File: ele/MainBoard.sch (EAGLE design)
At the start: 129 parts, among them IC1 MCP23017SP, IC2 74HC595D, IC3 74HC595D, X1 POWER_IN, X10 M7, X2 POWER_OUT, X3 M2, X4 M4, X5 M6, X6 M8, X7 M1, X8 M3, X9 M5

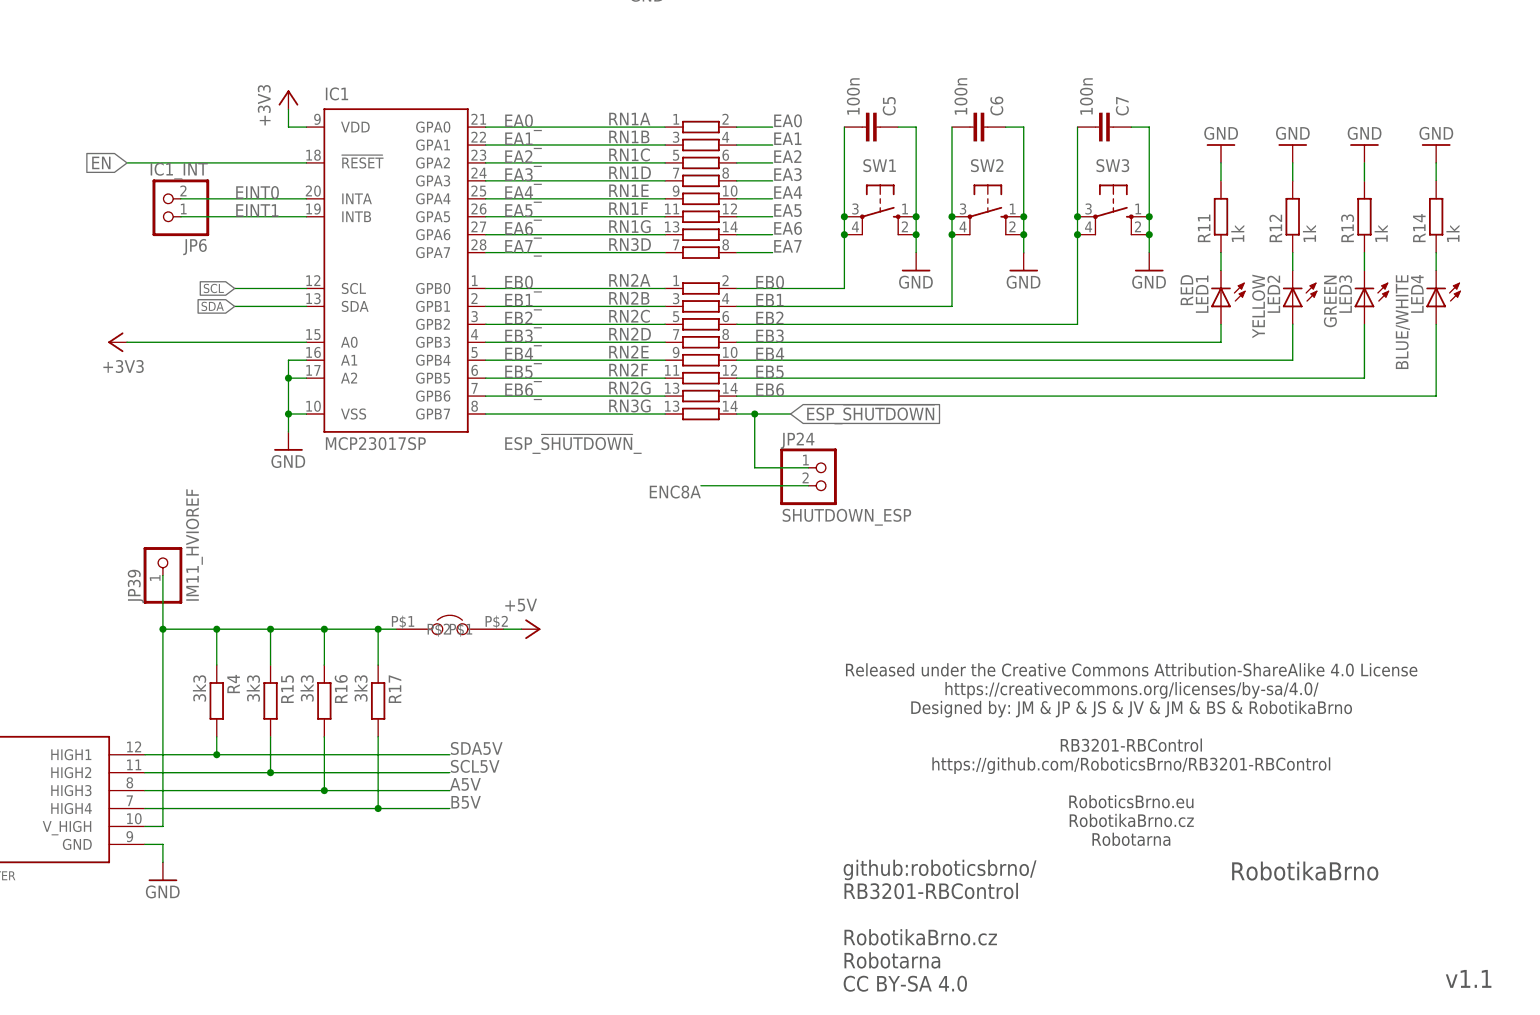
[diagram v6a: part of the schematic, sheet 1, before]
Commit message: ele: MainBoard - fix TO92 transistors pinout, change diodes package from SMD to TH, some signals routing improvements, fix some labels position, change version to 1.2
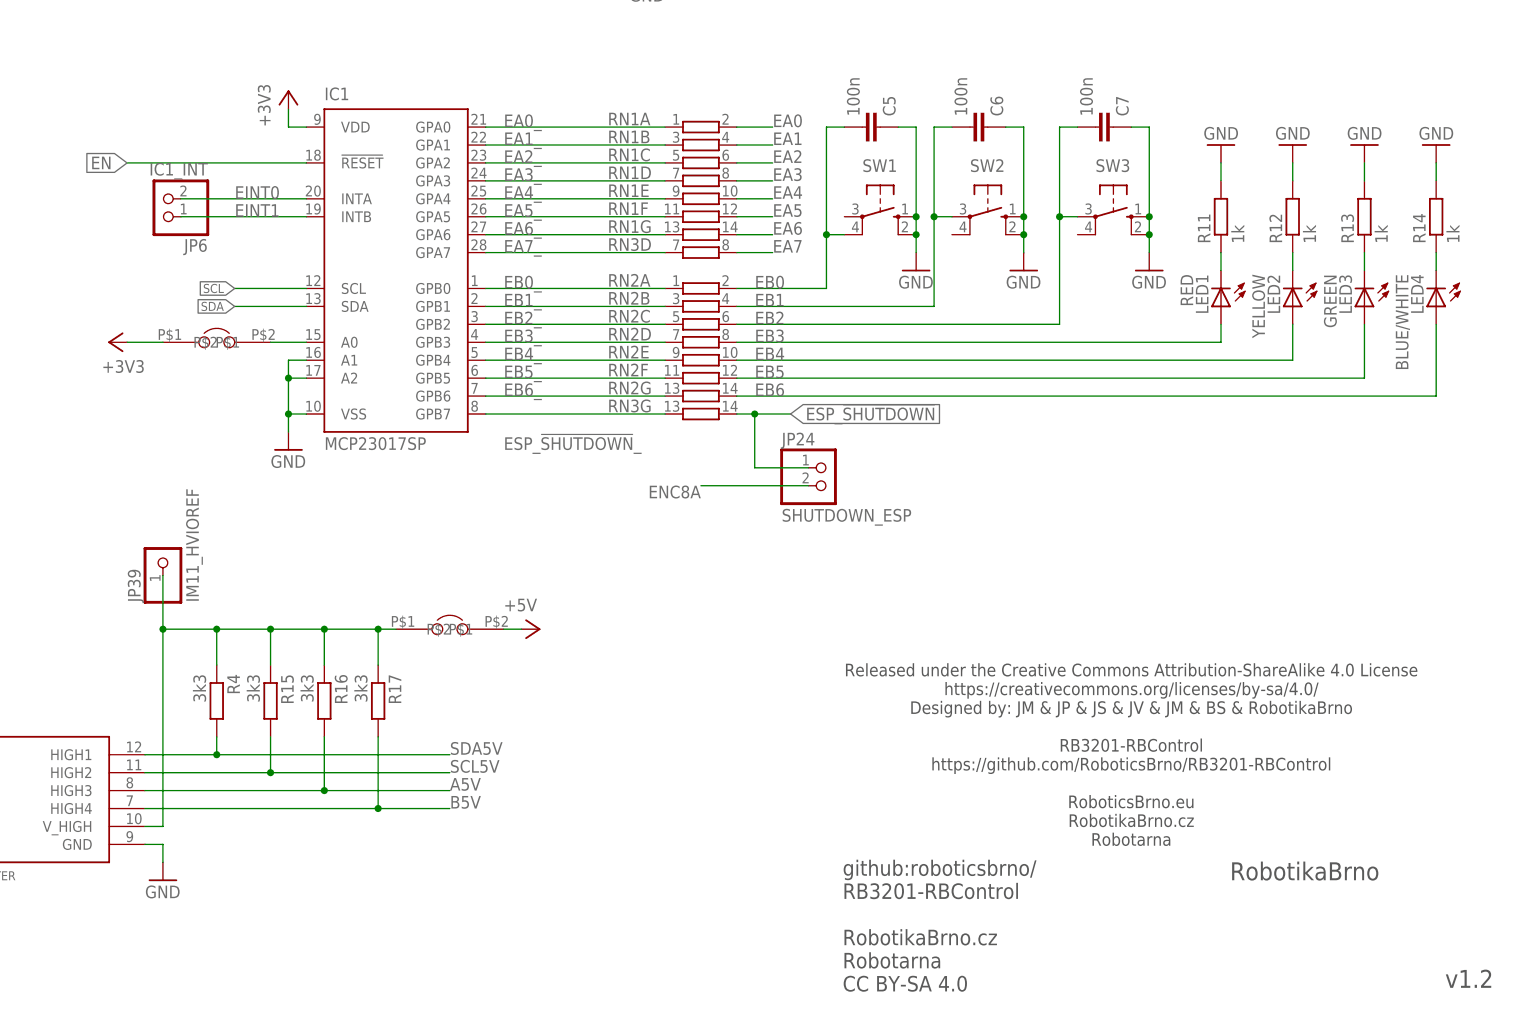
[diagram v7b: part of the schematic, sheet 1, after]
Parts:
- added U$1: SJ_NC, SolderJumperNormallyClosed:SJ_NC
- D1: device diode:DIODE-SOD123 -> diode:DIODE-D-2.5
- D2: device diode:DIODE-SOD123 -> diode:DIODE-D-7.5
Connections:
- new net EXP_A0: IC1.A0, U$1.P$2
- net +3V3: now also U$1.P$1; no longer IC1.A0
- net EB0: no longer SW1.P
- net EB1: no longer SW2.P1
- net EB2: no longer SW3.P1
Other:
- note added: "v1.2"

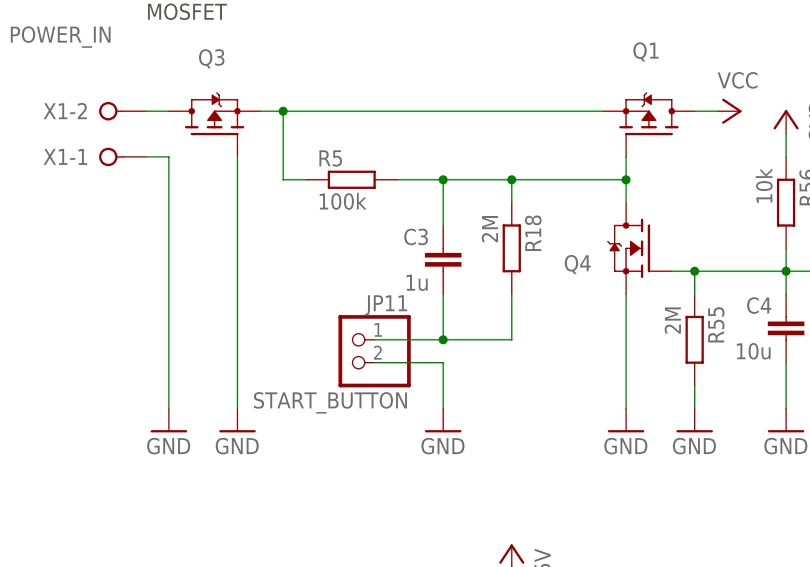
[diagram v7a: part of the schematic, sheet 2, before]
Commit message: ele: MainBoard - change value of C3 - from 1uF to 10uF
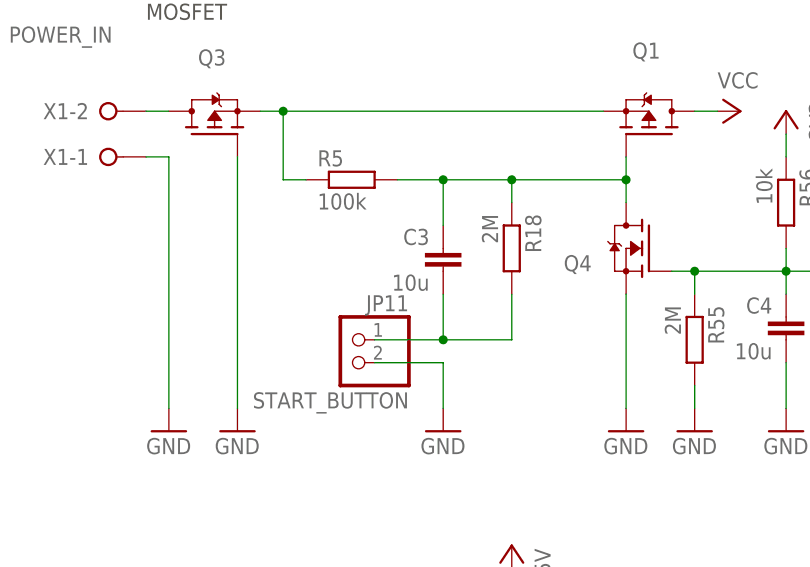
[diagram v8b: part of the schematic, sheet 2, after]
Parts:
- C3: value 1u -> 10u
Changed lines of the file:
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@@
 <grid distance="0.1" unitdist="inch" unit="inch" style="lines" multiple="1" display="no" altdistance="0.01" altunitdist="inch" altunit="inch"/>
 <layers>
-<layer number="1" name="Top" color="4" fill="1" visible="yes" active="no"/>
-<layer number="2" name="Route2" color="1" fill="3" visible="yes" active="no"/>
-<layer number="3" name="Route3" color="4" fill="3" visible="yes" active="no"/>
-<layer number="4" name="Route4" color="1" fill="4" visible="yes" active="no"/>
-<layer number="5" name="Route5" color="4" fill="4" visible="yes" active="no"/>
-<layer number="6" name="Route6" color="1" fill="8" visible="yes" active="no"/>
-<layer number="7" name="Route7" color="4" fill="8" visible="yes" active="no"/>
-<layer number="8" name="Route8" color="1" fill="2" visible="yes" active="no"/>
-<layer number="9" name="Route9" color="4" fill="2" visible="yes" active="no"/>
-<layer number="10" name="Route10" color="1" fill="7" visible="yes" active="no"/>
-<layer number="11" name="Route11" color="4" fill="7" visible="yes" active="no"/>
-<layer number="12" name="Route12" color="1" fill="5" visible="yes" active="no"/>
-<layer number="13" name="Route13" color="4" fill="5" visible="yes" active="no"/>
-<layer number="14" name="Route14" color="1" fill="6" visible="yes" active="no"/>
-<layer number="15" name="Route15" color="4" fill="6" visible="yes" active="no"/>
-<layer number="16" name="Bottom" color="1" fill="1" visible="yes" active="no"/>
-<layer number="17" name="Pads" color="2" fill="1" visible="yes" active="no"/>
-<layer number="18" name="Vias" color="2" fill="1" visible="yes" active="no"/>
-<layer number="19" name="Unrouted" color="6" fill="1" visible="yes" active="no"/>
-<layer number="20" name="Dimension" color="24" fill="1" visible="yes" active="no"/>
-<layer number="21" name="tPlace" color="7" fill="1" visible="yes" active="no"/>
-<layer number="22" name="bPlace" color="7" fill="1" visible="yes" active="no"/>
-<layer number="23" name="tOrigins" color="15" fill="1" visible="yes" active="no"/>
-<layer number="24" name="bOrigins" color="15" fill="1" visible="yes" active="no"/>
-<layer number="25" name="tNames" color="13" fill="1" visible="yes" active="no"/>
-<layer number="26" name="bNames" color="7" fill="1" visible="yes" active="no"/>
-<layer number="27" name="tValues" color="7" fill="1" visible="yes" active="no"/>
-<layer number="28" name="bValues" color="7" fill="1" visible="yes" active="no"/>
+<layer number="1" name="Top" color="4" fill="1" visible="no" active="no"/>
+<layer number="2" name="Route2" color="1" fill="3" visible="no" active="no"/>
+<layer number="3" name="Route3" color="4" fill="3" visible="no" active="no"/>
+<layer number="4" name="Route4" color="1" fill="4" visible="no" active="no"/>
+<layer number="5" name="Route5" color="4" fill="4" visible="no" active="no"/>
+<layer number="6" name="Route6" color="1" fill="8" visible="no" active="no"/>
+<layer number="7" name="Route7" color="4" fill="8" visible="no" active="no"/>
+<layer number="8" name="Route8" color="1" fill="2" visible="no" active="no"/>
+<layer number="9" name="Route9" color="4" fill="2" visible="no" active="no"/>
+<layer number="10" name="Route10" color="1" fill="7" visible="no" active="no"/>
+<layer number="11" name="Route11" color="4" fill="7" visible="no" active="no"/>
+<layer number="12" name="Route12" color="1" fill="5" visible="no" active="no"/>
+<layer number="13" name="Route13" color="4" fill="5" visible="no" active="no"/>
+<layer number="14" name="Route14" color="1" fill="6" visible="no" active="no"/>
+<layer number="15" name="Route15" color="4" fill="6" visible="no" active="no"/>
+<layer number="16" name="Bottom" color="1" fill="1" visible="no" active="no"/>
+<layer number="17" name="Pads" color="2" fill="1" visible="no" active="no"/>
+<layer number="18" name="Vias" color="2" fill="1" visible="no" active="no"/>
+<layer number="19" name="Unrouted" color="6" fill="1" visible="no" active="no"/>
+<layer number="20" name="Dimension" color="24" fill="1" visible="no" active="no"/>
+<layer number="21" name="tPlace" color="7" fill="1" visible="no" active="no"/>
+<layer number="22" name="bPlace" color="7" fill="1" visible="no" active="no"/>
+<layer number="23" name="tOrigins" color="15" fill="1" visible="no" active="no"/>
+<layer number="24" name="bOrigins" color="15" fill="1" visible="no" active="no"/>
+<layer number="25" name="tNames" color="13" fill="1" visible="no" active="no"/>
+<layer number="26" name="bNames" color="7" fill="1" visible="no" active="no"/>
+<layer number="27" name="tValues" color="7" fill="1" visible="no" active="no"/>
+<layer number="28" name="bValues" color="7" fill="1" visible="no" active="no"/>
 <layer number="29" name="tStop" color="7" fill="3" visible="no" active="no"/>
 <layer number="30" name="bStop" color="7" fill="6" visible="no" active="no"/>
@@
 <layer number="35" name="tGlue" color="7" fill="4" visible="no" active="no"/>
 <layer number="36" name="bGlue" color="7" fill="5" visible="no" active="no"/>
-<layer number="37" name="tTest" color="7" fill="1" visible="yes" active="no"/>
-<layer number="38" name="bTest" color="7" fill="1" visible="yes" active="no"/>
+<layer number="37" name="tTest" color="7" fill="1" visible="no" active="no"/>
+<layer number="38" name="bTest" color="7" fill="1" visible="no" active="no"/>
 <layer number="39" name="tKeepout" color="4" fill="11" visible="no" active="no"/>
 <layer number="40" name="bKeepout" color="1" fill="11" visible="no" active="no"/>
@@
 <layer number="44" name="Drills" color="7" fill="1" visible="no" active="no"/>
 <layer number="45" name="Holes" color="7" fill="1" visible="no" active="no"/>
-<layer number="46" name="Milling" color="3" fill="1" visible="yes" active="no"/>
-<layer number="47" name="Measures" color="7" fill="1" visible="yes" active="no"/>
-<layer number="48" name="Document" color="7" fill="1" visible="yes" active="no"/>
-<layer number="49" name="Reference" color="7" fill="1" visible="yes" active="no"/>
-<layer number="50" name="dxf" color="7" fill="1" visible="yes" active="no"/>
-<layer number="51" name="tDocu" color="7" fill="1" visible="yes" active="no"/>
-<layer number="52" name="bDocu" color="7" fill="1" visible="yes" active="no"/>
-<layer number="53" name="tGND_GNDA" color="7" fill="9" visible="yes" active="no"/>
-<layer number="54" name="bGND_GNDA" color="1" fill="9" visible="yes" active="no"/>
-<layer number="55" name="tPotisk" color="7" fill="1" visible="yes" active="no"/>
-<layer number="56" name="wert" color="7" fill="1" visible="yes" active="no"/>
-<layer number="57" name="tCAD" color="7" fill="1" visible="yes" active="no"/>
-<layer number="58" name="bNC" color="7" fill="1" visible="yes" active="no"/>
-<layer number="59" name="tCarbon" color="7" fill="1" visible="yes" active="no"/>
-<layer number="60" name="bCarbon" color="7" fill="1" visible="yes" active="no"/>
-<layer number="61" name="stand" color="7" fill="1" visible="yes" active="no"/>
+<layer number="46" name="Milling" color="3" fill="1" visible="no" active="no"/>
+<layer number="47" name="Measures" color="7" fill="1" visible="no" active="no"/>
+<layer number="48" name="Document" color="7" fill="1" visible="no" active="no"/>
+<layer number="49" name="Reference" color="7" fill="1" visible="no" active="no"/>
+<layer number="50" name="dxf" color="7" fill="1" visible="no" active="no"/>
+<layer number="51" name="tDocu" color="7" fill="1" visible="no" active="no"/>
+<layer number="52" name="bDocu" color="7" fill="1" visible="no" active="no"/>
+<layer number="53" name="tGND_GNDA" color="7" fill="9" visible="no" active="no"/>
+<layer number="54" name="bGND_GNDA" color="1" fill="9" visible="no" active="no"/>
+<layer number="55" name="tPotisk" color="7" fill="1" visible="no" active="no"/>
+<layer number="56" name="wert" color="7" fill="1" visible="no" active="no"/>
+<layer number="57" name="tCAD" color="7" fill="1" visible="no" active="no"/>
+<layer number="58" name="bNC" color="7" fill="1" visible="no" active="no"/>
+<layer number="59" name="tCarbon" color="7" fill="1" visible="no" active="no"/>
+<layer number="60" name="bCarbon" color="7" fill="1" visible="no" active="no"/>
+<layer number="61" name="stand" color="7" fill="1" visible="no" active="no"/>
 <layer number="88" name="SimResults" color="9" fill="1" visible="yes" active="yes"/>
 <layer number="89" name="SimProbes" color="9" fill="1" visible="yes" active="yes"/>
@@
 <part name="R14" library="resistor" library_urn="urn:adsk.eagle:library:348" deviceset="R-EU_" device="0204/2V" package3d_urn="urn:adsk.eagle:package:25948/1" value="1k"/>
 <part name="GND39" library="supply1" library_urn="urn:adsk.eagle:library:371" deviceset="GND" device=""/>
-<part name="C3" library="rcl_upravena" deviceset="C-EU" device="C1206" value="1u"/>
+<part name="C3" library="rcl_upravena" deviceset="C-EU" device="C1206" value="10u"/>
 <part name="IM11" library="LevelShifter" deviceset="LEVEL_SHIFTER" device=""/>
 <part name="GND40" library="supply1" library_urn="urn:adsk.eagle:library:371" deviceset="GND" device=""/>
